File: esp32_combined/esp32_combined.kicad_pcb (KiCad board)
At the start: 2 copper layers, 71.2 x 33.1 mm, 28 parts, among them J1 JST B7B-ZR, J2 JST B7B-ZR, J3 JST B6B-PH-K-S, J4 XT30U-M, J5 JST B5B-ZR, J6 DNP, J8 JST B6B-ZR, J9 JST B6B-ZR, SW1 SS12D10, U1 ESP32 DEV KIT Module 30-pin, U2 LM2596 Module

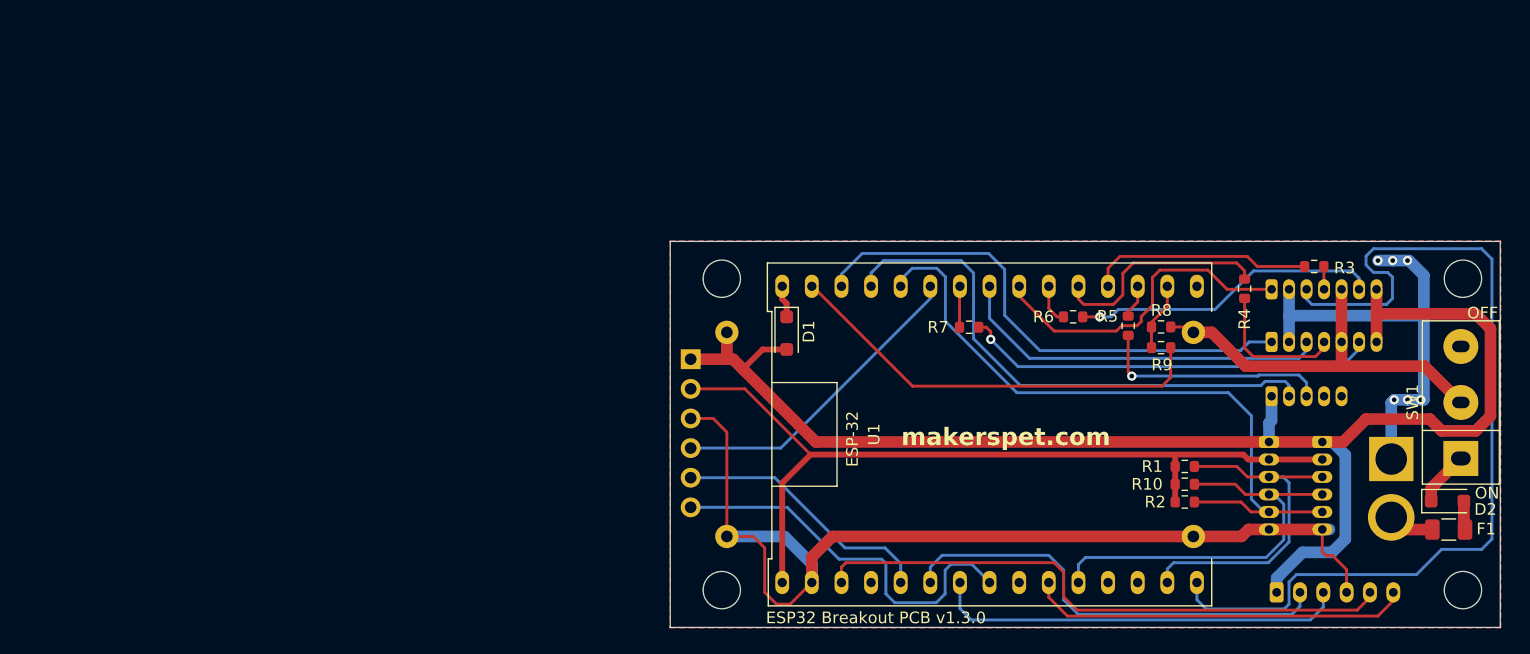
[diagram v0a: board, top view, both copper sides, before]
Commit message: Dual headers
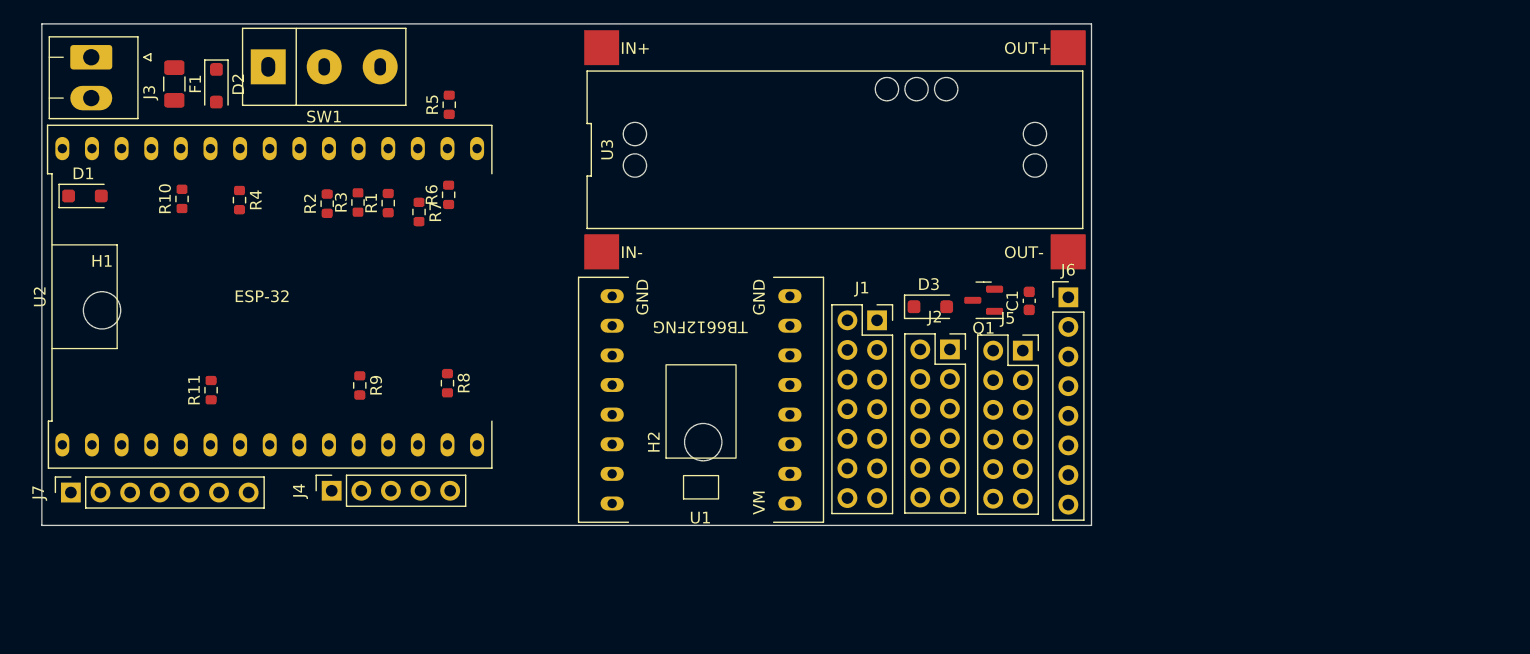
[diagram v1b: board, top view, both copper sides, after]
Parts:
- removed H3, H4: MountingHole, MountingHole:MountingHole_3.2mm_M3
- removed J8, J9: JST B6B-ZR, Makerspet:JST_ZH_B6B-ZR_1x06_P1.50mm_Vertical
- added C1: 22uF, Capacitor_SMD:C_0603_1608Metric, F.Cu at (124.7, 53.7)
- added D3: FS26, Diode_SMD:D_SOD-123F, F.Cu at (116.2, 54.3)
- added J7: HDR SKT 7PIN VERT 2.54MM, Connector_PinSocket_2.54mm:PinSocket_1x07_P2.54mm_Vertical, F.Cu at (42.5, 70.2)
- added Q1: AS2302, Package_TO_SOT_SMD:SOT-23, F.Cu at (120.8, 53.7)
- added R11: 10k, Resistor_SMD:R_0603_1608Metric, F.Cu at (54.5, 61.4)
- added U3: LM2596 Module, Makerspet:LM2596 Module SMD, F.Cu at (108.0, 40.8)
- J1: value JST B7B-ZR -> SKT 2x7PIN VERT 2.54MM; footprint Makerspet:JST_ZH_B7B-ZR_1x07_P1.50mm_Vertical -> Connector_PinSocket_2.54mm:PinSocket_2x07_P2.54mm_Vertical; moved to F.Cu
- J2: value JST B7B-ZR -> SKT 2x6PIN VERT 2.54MM; footprint Makerspet:JST_ZH_B7B-ZR_1x07_P1.50mm_Vertical -> Connector_PinSocket_2.54mm:PinSocket_2x06_P2.54mm_Vertical; moved to F.Cu
- J3: value JST B6B-PH-K-S -> TERM BLK 3.5MM 2P SIDE; footprint Connector_JST:JST_PH_B6B-PH-K_1x06_P2.00mm_Vertical -> Makerspet:Terminal_Block_2p_3.5mm_SideEntry; moved to F.Cu
- J4: value XT30U-M -> HDR SKT 5PIN VERT 2.54MM; footprint Makerspet:AMASS_XT30U-F_1x02_P5.0mm_Vertical -> Connector_PinSocket_2.54mm:PinSocket_1x05_P2.54mm_Vertical; moved to F.Cu
- J5: value JST B5B-ZR -> SKT 2x6PIN VERT 2.54MM; footprint Makerspet:JST_ZH_B5B-ZR_1x05_P1.50mm_Vertical -> Connector_PinSocket_2.54mm:PinSocket_2x06_P2.54mm_Vertical; moved to F.Cu
- J6: value DNP -> HDR SKT 8PIN VERT 2.54MM; footprint Connector_PinSocket_2.54mm:PinSocket_1x06_P2.54mm_Vertical -> Connector_PinHeader_2.54mm:PinHeader_1x08_P2.54mm_Vertical; moved to F.Cu
- R5: value 10k -> 200k
- R6: value 10k -> 20k
- R8: value 200k -> 10k
- R9: value 20k -> 10k
- U1: value ESP32 DEV KIT Module 30-pin -> TB6612FNG Module; footprint Makerspet:ESP-32 -> Makerspet:TB6612FNG Module
- U2: value LM2596 Module -> ESP32 DEV KIT Module 30-pin; footprint Makerspet:LM2596 Module -> Makerspet:ESP-32; moved to F.Cu
- moved F1 115.8 mm to (51.4, 35.2), turned to -90 degrees
- moved J3 111.5 mm to (44.2, 32.9), turned to -90 degrees
- moved D2 111.4 mm to (55.0, 35.3), turned to -90 degrees
- moved SW1 101.6 mm to (64.2, 33.7), turned to 0 degrees
- moved J4 90.9 mm to (64.9, 70.0), turned to 90 degrees
- moved R10 89.4 mm to (52.0, 45.0), turned to 90 degrees
- moved R4 86.5 mm to (56.9, 45.1)
- moved R3 82.2 mm to (67.1, 45.3), turned to 90 degrees
- moved R2 77.9 mm to (64.5, 45.4), turned to 90 degrees
- moved R1 71.9 mm to (69.7, 45.4), turned to 90 degrees
- moved R9 68.8 mm to (67.3, 61.0), turned to -90 degrees
- moved H2 66.6 mm to (96.7, 65.9), turned to 90 degrees
- moved R8 61.4 mm to (74.8, 60.8), turned to -90 degrees
- moved D1 61.3 mm to (43.7, 44.8), turned to 0 degrees
- moved R5 61.2 mm to (74.9, 36.9), turned to 90 degrees
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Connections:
- F1 pad 1: Net-(J4-+) -> Net-(J3-Pin_1)
- J1 pad 1: /MOT_PWM_RIGHT_IN3 -> /MOT+RIGHT
- J1 pad 2: GND -> /MOT-RIGHT
- J1 pad 3: /MOT_CW_RIGHT_IN4 -> GND
- J1 pad 4: Net-(J1-Pin_4) -> /M_FG_RIGHT_ENC_A
- J1 pad 5: Vdrive -> /M_RIGHT_ENC_B
- J1 pad 6: Net-(J1-Pin_6) -> +5V
- J1 pad 7: +5V -> GND
- J2 pad 1: /MOT_PWM_LEFT_IN1 -> GND
- J2 pad 2: GND -> Vdrive
- J2 pad 3: /MOT_CW_LEFT_IN2 -> GND
- J2 pad 4: Net-(J2-Pin_4) -> /M_FG_RIGHT_ENC_A
- J2 pad 5: Vdrive -> /MOT_PWM_RIGHT_IN1
- J2 pad 6: Net-(J2-Pin_6) -> /MOT_CW_RIGHT_IN2
- J2 pad 7: +5V -> /MOT_CW_LEFT_IN2
- J3 pad 1: +5V -> Net-(J3-Pin_1)
- J3 pad 2: /LDS_TX -> GND
- J4 pad 2: Net-(J4-+) -> GND
- J5 pad 1: +5V -> GND
- J5 pad 2: /GPIO12_OUT_STRAP -> GND
- J5 pad 3: Net-(J5-Pin_3) -> +5V
- J5 pad 4: GND -> /I2C_SCL
- J5 pad 5: GND -> /I2C_SDA
- J6 pad 1: +5V -> GND
- J6 pad 2: +3V3 -> GND
- J6 pad 3: GND -> +5V
- J6 pad 4: /GPIO27 -> Net-(D3-A)
- J6 pad 5: /GPIO4 -> Net-(J6-Pin_5)
- J6 pad 6: /GPIO5_BOOT_STRAP -> /LDS_MOT_PWM
- R1 pad 1: +3V3 -> /MOT_FG_LEFT_ENC_A
- R1 pad 2: /I2C_SCL -> /M_FG_LEFT_ENC_A
- R10 pad 2: /I2C_SDA -> /I2C_INT
- R2 pad 1: +3V3 -> /MOT_LEFT_ENC_B
- R2 pad 2: /I2C_INT -> /M_LEFT_ENC_B
- R3 pad 1: /MOT_FG_LEFT_ENC_A -> /MOT_FG_RIGHT_ENC_A
- R3 pad 2: Net-(J2-Pin_4) -> /M_FG_RIGHT_ENC_A
- R4 pad 1: /MOT_FG_RIGHT_ENC_A -> /MOT_RIGHT_ENC_B
- R4 pad 2: Net-(J1-Pin_4) -> /M_RIGHT_ENC_B
- R5 pad 1: /GPIO39_IN -> /BAT_ADC
- R5 pad 2: Net-(J5-Pin_3) -> Vdrive
- R6 pad 1: /ENC_B_LEFT -> GND
- R6 pad 2: Net-(J2-Pin_6) -> /BAT_ADC
- R7 pad 1: /ENC_B_RIGHT -> /GPIO39_IN
- R7 pad 2: Net-(J1-Pin_6) -> Net-(J4-Pin_3)
- R8 pad 1: /BAT_ADC -> +3V3
- R8 pad 2: Vdrive -> /I2C_SCL
- R9 pad 1: GND -> +3V3
- R9 pad 2: /BAT_ADC -> /I2C_SDA
- U1 pad 1: +3V3 -> Vdrive
- U1 pad 10: /LDS_EN -> +5V
- U1 pad 11: /I2C_SDA -> /MOT_CW_LEFT_IN2
- U1 pad 12: unconnected-(U1-CP2102_GPIO3/UART0_RX-Pad12) -> /MOT_PWM_LEFT_IN1
- U1 pad 13: unconnected-(U1-CP2102_GPIO1/UART0_TX-Pad13) -> +5V
- U1 pad 14: /I2C_SCL -> /MOT_PWM_RIGHT_IN1
- U1 pad 15: /MOT_CW_LEFT_IN2 -> /MOT_CW_RIGHT_IN2
- U1 pad 16: unconnected-(U1-EN-Pad16) -> +5V
- U1 pad 2: GND -> +5V
- U1 pad 3: /LDS_MOT_PWM -> GND
- U1 pad 4: unconnected-(U1-LED_GPIO2/ADC2_C2/TOUCH2/RTC_GPIO12-Pad4) -> /MOT+RIGHT
- U1 pad 5: /GPIO4 -> /MOT-RIGHT
- U1 pad 6: /LDS_TX -> /MOT+LEFT
- U1 pad 7: /LDS_RX -> /MOT-LEFT
- U1 pad 8: /GPIO5_BOOT_STRAP -> GND
- U1 pad 9: /SERVO_REAR -> GND
- U2 pad 1: GND -> +3V3
- U2 pad 3: +5V -> /LDS_MOT_PWM
- U2 pad 4: Vdrive -> unconnected-(U2-LED_GPIO2/ADC2_C2/TOUCH2/RTC_GPIO12-Pad4)
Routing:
- net GND: track 166.2 -> 0.00 mm, vias 6 -> 0
- net +5V: track 124.6 -> 0.00 mm
- net /MOT_CW_LEFT_IN2: track 80.0 -> 0.00 mm
- net +3V3: track 73.1 -> 0.00 mm
- net /I2C_INT: track 58.9 -> 0.00 mm
- net /LDS_MOT_PWM: track 50.5 -> 0.00 mm
- net /GPIO12_OUT_STRAP: track 46.4 -> 0.00 mm
- net /MOT_PWM_RIGHT_IN3: track 44.7 -> 0.00 mm
- net /LDS_TX: track 38.4 -> 0.00 mm
- net /I2C_SDA: track 36.0 -> 0.00 mm
- net Net-(J1-Pin_6): track 35.6 -> 0.00 mm, vias 1 -> 0
- net /LDS_RX: track 35.6 -> 0.00 mm
- net Vdrive: track 34.2 -> 0.00 mm
- net /GPIO5_BOOT_STRAP: track 33.7 -> 0.00 mm
- net /LDS_EN: track 32.7 -> 0.00 mm
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- removed copper zone on F.Cu, net GND
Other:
- board size 71.2 x 33.1 mm -> 90 x 43 mm
- board text removed: "+BATT"
- board text removed: "ESP32 Breakout PCB v1.3.0"
- board text removed: "EXP"
- board text removed: "L MOTOR R"
- board text removed: "LASER DIST"
- board text removed: "LM2596 DC-DC Module"
- board text removed: "OFF"
- board text removed: "ON"
- board text removed: "U.DIST"
- board text removed: "makerspet.com"

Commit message: Labels space
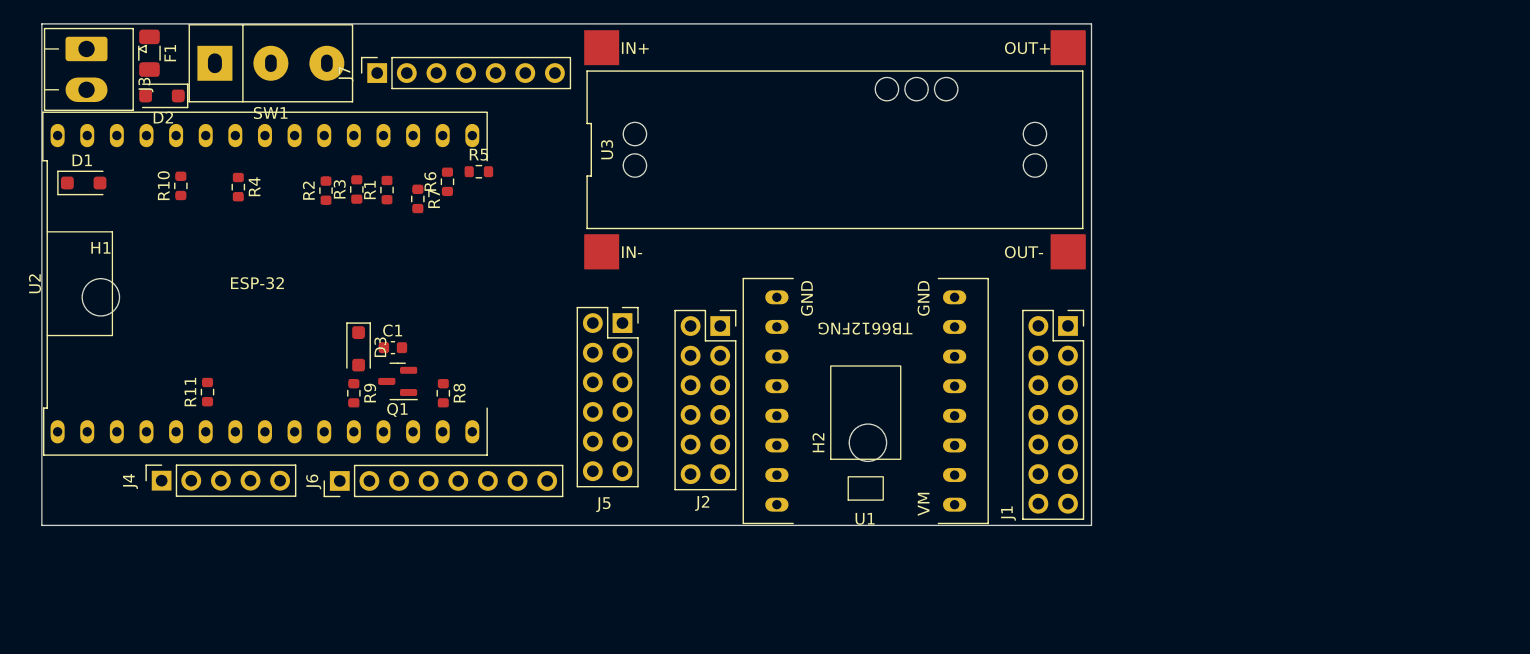
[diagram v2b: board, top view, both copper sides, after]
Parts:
- moved J6 64.4 mm to (65.5, 69.2), turned to 90 degrees
- moved C1 54.7 mm to (70.1, 57.8), turned to 0 degrees
- moved Q1 50.7 mm to (70.5, 60.7)
- moved D3 49.2 mm to (67.2, 57.9), turned to -90 degrees
- moved J7 44.5 mm to (68.8, 34.2)
- moved J5 34.4 mm to (89.8, 55.7)
- moved J2 19.8 mm to (98.2, 55.9)
- moved J1 16.4 mm to (128.0, 55.9)
- moved J4 14.6 mm to (50.3, 69.2)
- moved U1 14.1 mm to (110.6, 62.3)
- moved H2 14.1 mm to (110.8, 65.9)
- moved R5 6.28 mm to (77.5, 42.7), turned to 0 degrees
- moved D2 4.75 mm to (50.3, 36.2), turned to 180 degrees
- moved SW1 4.58 mm to (59.6, 33.4)
- moved F1 3.40 mm to (49.2, 32.5)
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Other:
- board text added: "18"
- board text added: "27"
- board text added: "4"
- board text added: "5"
- board text added: "5V"
- board text added: "A B"
- board text added: "BRUSHED MOTORS"
- board text added: "BRUSHLESS MOTORS"
- board text added: "EXPANSION"
- board text added: "GND"
- board text added: "LT RT"
- board text added: "LiDAR SENSOR"
- board text added: "U/S DIST SENSOR"

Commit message: ESP32 Combined Gerber
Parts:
- added C2: 100uF 16V, Capacitor_Tantalum_SMD:CP_EIA-7343-15_Kemet-W, F.Cu at (114.1, 68.2)
- added H3: MountingHole, MountingHole:MountingHole_3.2mm_M3, F.Cu at (82.0, 40.3)
- J6: footprint Connector_PinHeader_2.54mm:PinHeader_1x08_P2.54mm_Vertical -> Connector_PinSocket_2.54mm:PinSocket_1x08_P2.54mm_Vertical
- moved D1 26.4 mm to (69.2, 37.0)
- moved H1 6.71 mm to (43.9, 60.0)
- moved H2 4.79 mm to (109.2, 61.4)
- moved F1 2.69 mm to (49.2, 35.2)
- moved R7 1.85 mm to (71.8, 43.2)
- moved D2 1.48 mm to (51.5, 35.3), turned to -90 degrees
- moved R2 1.11 mm to (64.2, 43.2), turned to -90 degrees
- moved R1 1.09 mm to (69.3, 43.2), turned to -90 degrees
- moved R3 1.03 mm to (66.8, 43.2), turned to -90 degrees
- moved R4 0.83 mm to (56.6, 43.2)
- moved R5 0.82 mm to (76.7, 42.4)
- moved R10 0.80 mm to (51.5, 43.2)
- moved R6 0.53 mm to (74.4, 43.2)
- moved J7 0.25 mm to (68.8, 34.0)
- moved J5 0.25 mm to (89.8, 55.9)
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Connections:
- J1 pad 1: /MOT+RIGHT -> /MOT+LEFT
- J1 pad 10: /M_LEFT_ENC_B -> /M_RIGHT_ENC_B
- J1 pad 11: /M_FG_LEFT_ENC_A -> +5V
- J1 pad 12: GND -> +5V
- J1 pad 13: /MOT-LEFT -> GND
- J1 pad 14: /MOT+LEFT -> GND
- J1 pad 2: /MOT-RIGHT -> /MOT+RIGHT
- J1 pad 3: GND -> /MOT-LEFT
- J1 pad 4: /M_FG_RIGHT_ENC_A -> /MOT-RIGHT
- J1 pad 5: /M_RIGHT_ENC_B -> GND
- J1 pad 6: +5V -> GND
- J1 pad 7: GND -> /M_FG_LEFT_ENC_A
- J1 pad 8: GND -> /M_FG_RIGHT_ENC_A
- J1 pad 9: +5V -> /M_LEFT_ENC_B
- J2 pad 10: GND -> /MOT_PWM_RIGHT_IN1
- J2 pad 11: Vdrive -> /MOT_CW_LEFT_IN2
- J2 pad 12: GND -> /MOT_CW_RIGHT_IN2
- J2 pad 2: Vdrive -> GND
- J2 pad 3: GND -> Vdrive
- J2 pad 4: /M_FG_RIGHT_ENC_A -> Vdrive
- J2 pad 5: /MOT_PWM_RIGHT_IN1 -> GND
- J2 pad 6: /MOT_CW_RIGHT_IN2 -> GND
- J2 pad 7: /MOT_CW_LEFT_IN2 -> /M_FG_LEFT_ENC_A
- J2 pad 8: /MOT_PWM_LEFT_IN1 -> /M_FG_RIGHT_ENC_A
- J2 pad 9: /M_FG_LEFT_ENC_A -> /MOT_PWM_LEFT_IN1
- J5 pad 10: +5V -> /I2C_SDA
- J5 pad 11: GND -> /I2C_INT
- J5 pad 12: GND -> /I2C_INT
- J5 pad 3: +5V -> GND
- J5 pad 4: /I2C_SCL -> GND
- J5 pad 5: /I2C_SDA -> +5V
- J5 pad 6: /I2C_INT -> +5V
- J5 pad 7: /I2C_INT -> /I2C_SCL
- J5 pad 8: /I2C_SDA -> /I2C_SCL
- J5 pad 9: /I2C_SCL -> /I2C_SDA
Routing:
- net +5V: track 0.00 -> 217.0 mm, vias 0 -> 4
- net Vdrive: track 0.00 -> 130.9 mm
- net /M_LEFT_ENC_B: track 0.00 -> 119.2 mm
- net /M_RIGHT_ENC_B: track 0.00 -> 94.8 mm
- net /MOT_PWM_RIGHT_IN1: track 0.00 -> 86.2 mm
- net /M_FG_LEFT_ENC_A: track 0.00 -> 79.2 mm
- net /M_FG_RIGHT_ENC_A: track 0.00 -> 74.1 mm
- net +3V3: track 0.00 -> 66.6 mm
- net /LDS_MOT_PWM: track 0.00 -> 64.9 mm
- net /MOT_CW_RIGHT_IN2: track 0.00 -> 59.3 mm
- net /GPIO12_OUT_STRAP: track 0.00 -> 57.6 mm
- net /MOT_PWM_LEFT_IN1: track 0.00 -> 56.9 mm
- net GND: track 0.00 -> 56.8 mm, vias 0 -> 10
- net /GPIO4: track 0.00 -> 56.0 mm, vias 0 -> 2
- net /MOT_CW_LEFT_IN2: track 0.00 -> 55.3 mm
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- added copper zone on B.Cu, net GND
- added copper zone on F.Cu, net GND
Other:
- board text added: "+BAT"
- board text added: "MAKERSPET.COM"
- board text added: "OFF"
- board text added: "ON"
- board text added: "[USB]"
- board text added: "v0.1.0"
